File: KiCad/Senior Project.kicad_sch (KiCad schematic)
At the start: 16 parts, among them J1 USB_C_Receptacle_USB2.0_16P, J2 Screw_Terminal_01x02, J3 Screw_Terminal_01x06, J4 Conn_ARM_JTAG_SWD_10, SW1 SW_Push, U1 ESP32-S3-WROOM-1

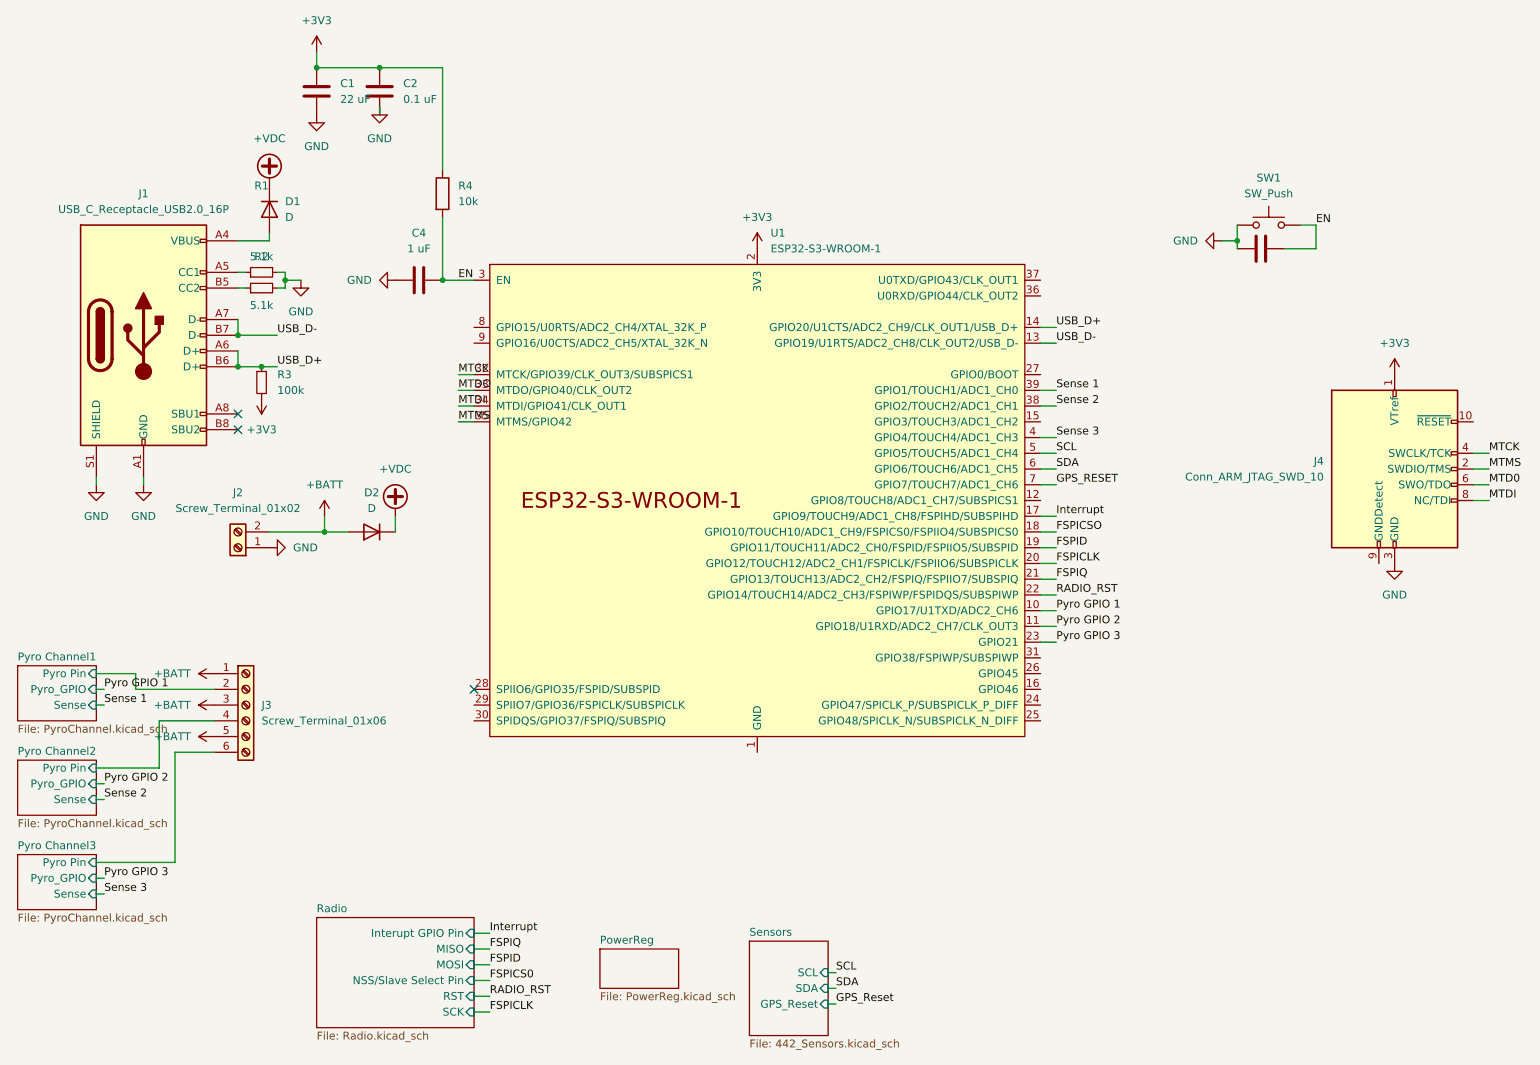
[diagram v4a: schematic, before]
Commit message: Finished base schematic and pin connections, need to add test pins
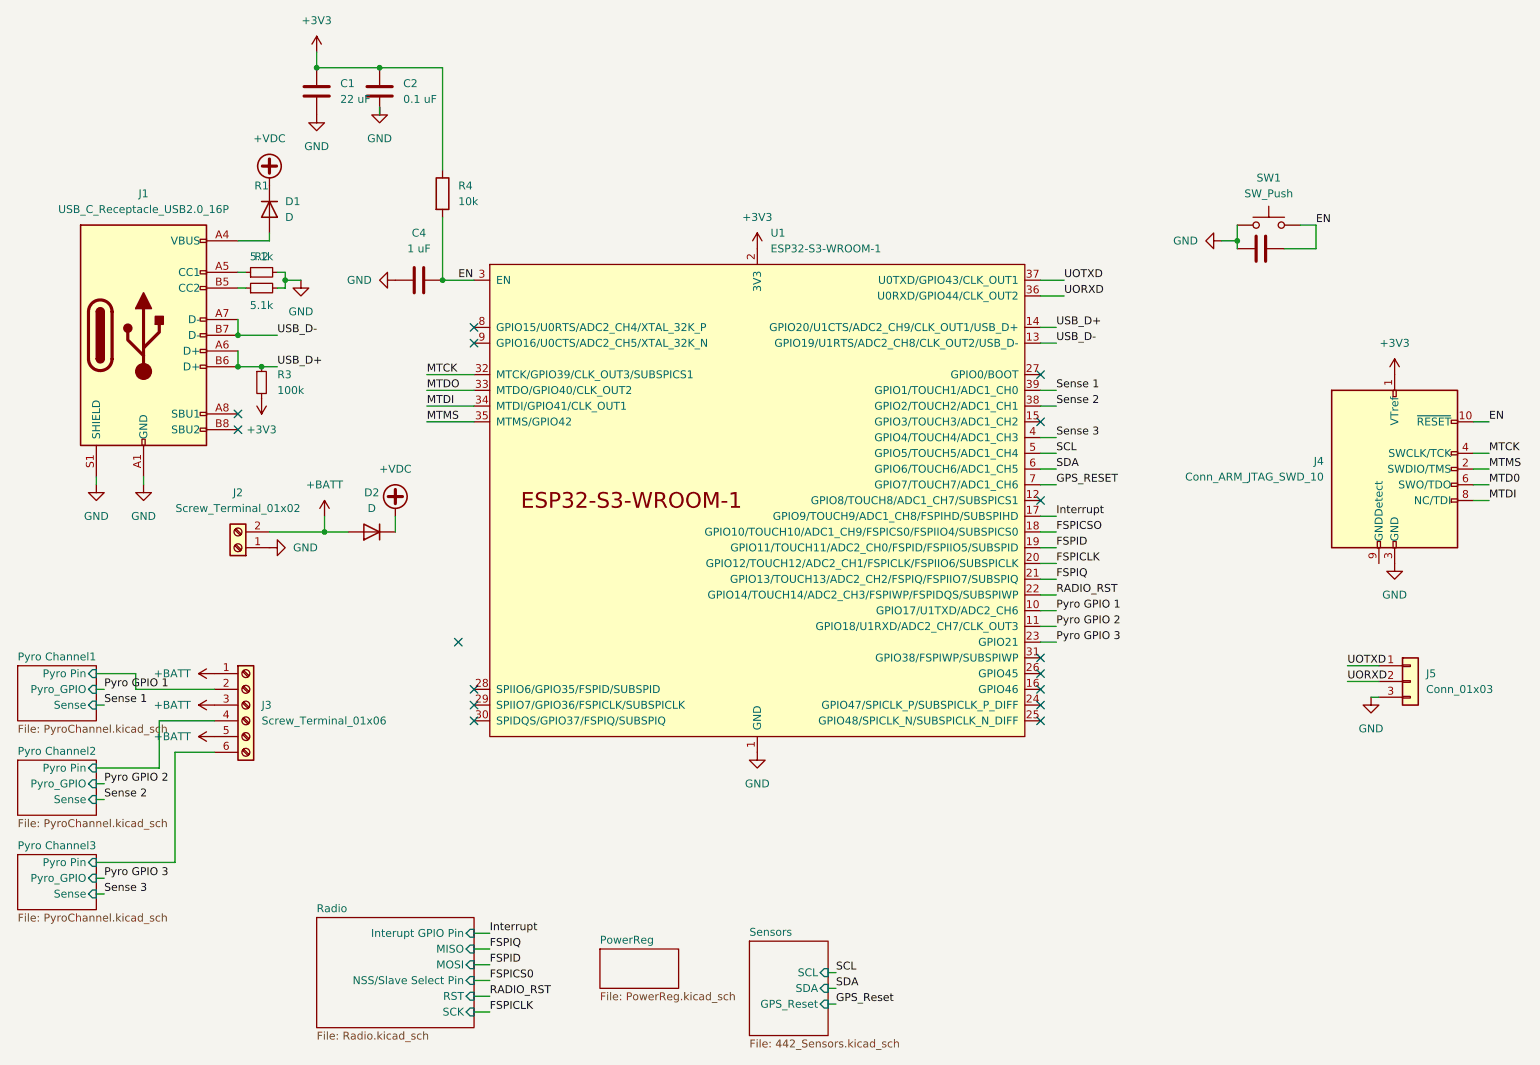
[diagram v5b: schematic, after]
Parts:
- added J5: Conn_01x03, symbol Connector_Generic:Conn_01x03
- J1: footprint Connector_USB:USB_C_Receptacle_JAE_DX07S016JA1R1500 -> USB4105_GF_A (1):GCT_USB4105-GF-A
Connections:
- net EN: now also J4.10 (~{RESET})
- net GND: now also U1.1 (GND), U1.40 (GND), U1.41 (GND), J5.3 (Pin_3)
- net UORXD: now reaches U1.36 (U0RXD/GPIO44/CLK_OUT2)
- net UORXD: now also J5.2 (Pin_2)
- net UOTXD: now reaches U1.37 (U0TXD/GPIO43/CLK_OUT1)
- net UOTXD: now also J5.1 (Pin_1)
- no-connect marks 3 -> 16

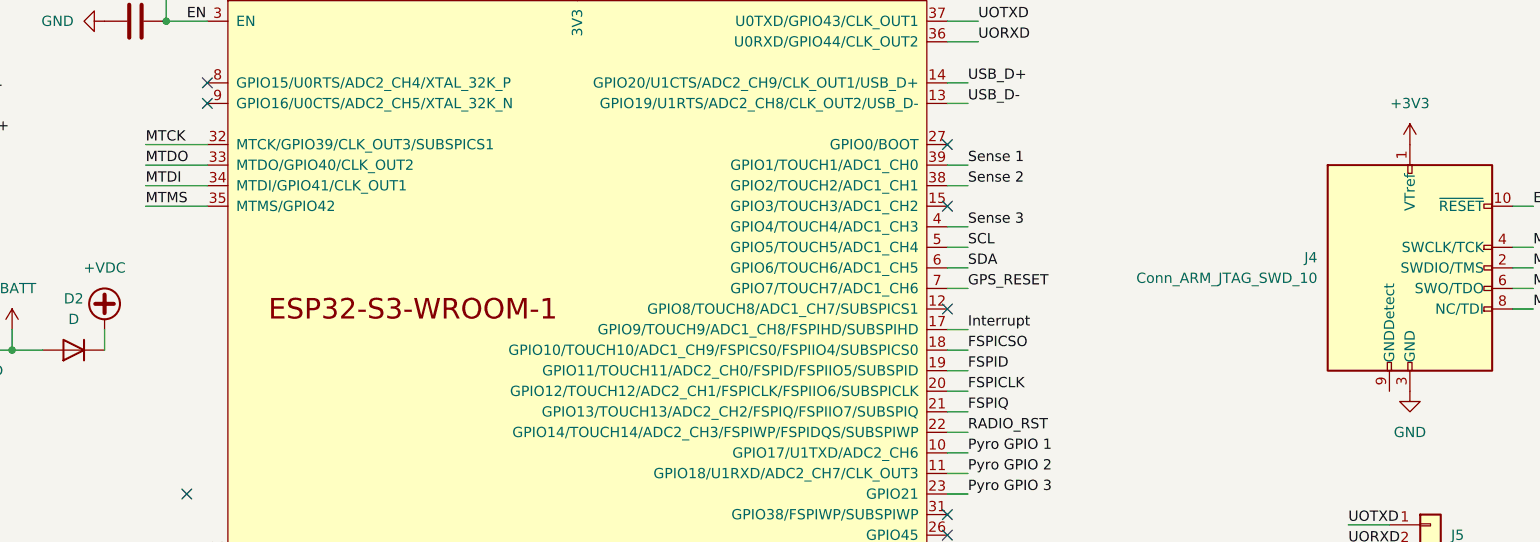
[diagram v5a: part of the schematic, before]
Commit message: ERC fixes and assigned footprints
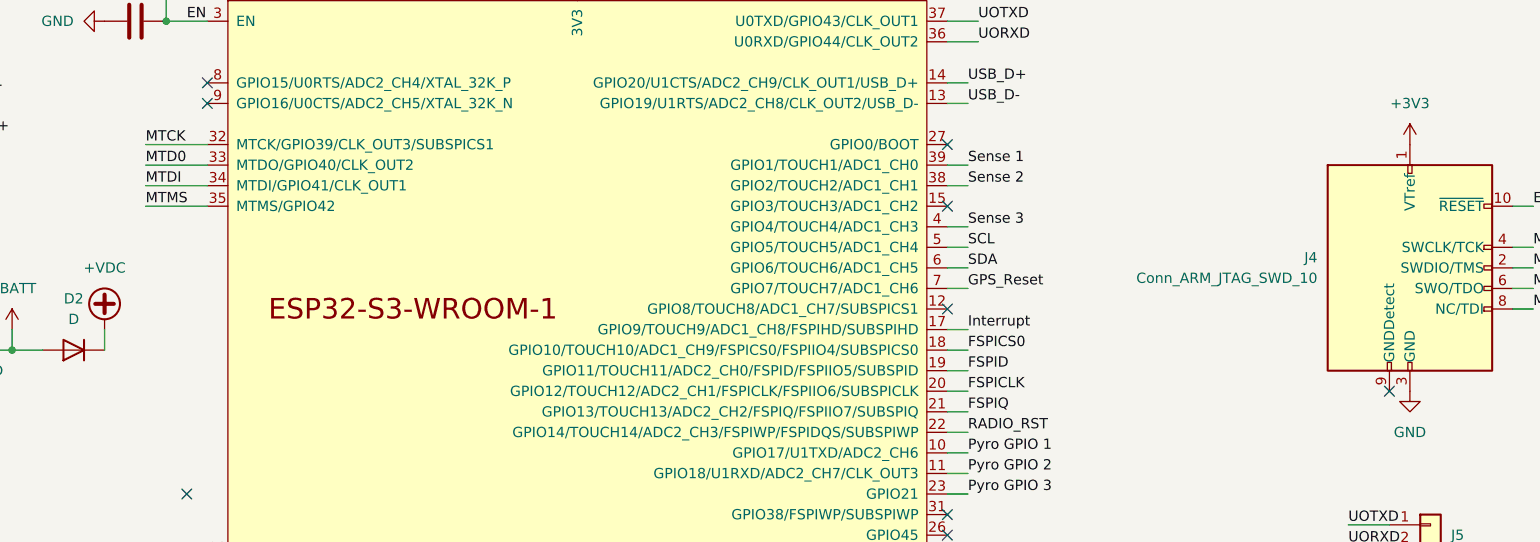
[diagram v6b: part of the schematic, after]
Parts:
- R4: footprint (none) -> Resistor_SMD:R_0402_1005Metric
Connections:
- net FSPICSO is gone; now on net FSPICS0: U1.18 (GPIO10/TOUCH10/ADC1_CH9/FSPICS0/FSPIIO4/SUBSPICS0)
- net GPS_RESET is gone; now on net GPS_Reset: U1.7 (GPIO7/TOUCH7/ADC1_CH6)
- net MTDO is gone; now on net MTD0: U1.33 (MTDO/GPIO40/CLK_OUT2)
- no-connect marks 16 -> 17
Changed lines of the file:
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@@
 	)
 	(no_connect
+		(at 248.92 101.6)
+	)
+	(no_connect
 		(at 102.87 127)
 	)
@@
 	(wire
 		(pts
-			(xy 95.25 73.66) (xy 102.87 73.66)
-		)
-		(stroke
-			(width 0)
-			(type default)
-		)
-	)
-	(wire
-		(pts
 			(xy 41.91 87.63) (xy 41.91 88.9)
 		)
@@
 	(wire
 		(pts
+			(xy 95.25 73.66) (xy 102.87 73.66)
+		)
+		(stroke
+			(width 0)
+			(type default)
+		)
+	)
+	(wire
+		(pts
 			(xy 69.85 48.26) (xy 69.85 49.53)
 		)
@@
 		)
 	)
+	(label "MTD0"
+		(at 95.25 73.66 0)
+		(effects
+			(font
+				(size 1.27 1.27)
+			)
+			(justify left bottom)
+		)
+	)
 	(label "MTCK"
 		(at 95.25 71.12 0)
@@
 		)
 	)
-	(label "GPS_RESET"
+	(label "GPS_Reset"
 		(at 196.85 88.9 0)
 		(effects
@@
 		)
 	)
-	(label "MTDO"
-		(at 95.25 73.66 0)
-		(effects
-			(font
-				(size 1.27 1.27)
-			)
-			(justify left bottom)
-		)
-	)
 	(label "MTMS"
 		(at 95.25 78.74 0)
@@
 		)
 	)
-	(label "FSPICSO"
+	(label "FSPICS0"
 		(at 196.85 96.52 0)
 		(effects
@@
 			)
 		)
-		(property "Footprint" ""
+		(property "Footprint" "Resistor_SMD:R_0402_1005Metric"
 			(at 96.012 41.91 90)
 			(effects

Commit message: More footprints assigned
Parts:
- C1, C2, C3, C4: footprint (none) -> Capacitor_SMD:C_0402_1005Metric
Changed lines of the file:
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@@
 			)
 		)
-		(property "Footprint" ""
+		(property "Footprint" "Capacitor_SMD:C_0402_1005Metric"
 			(at 78.4352 29.21 0)
 			(effects
@@
 			)
 		)
-		(property "Footprint" ""
+		(property "Footprint" "Capacitor_SMD:C_0402_1005Metric"
 			(at 233.68 49.8348 0)
 			(effects
@@
 			)
 		)
-		(property "Footprint" ""
+		(property "Footprint" "Capacitor_SMD:C_0402_1005Metric"
 			(at 97.79 54.9148 0)
 			(effects
@@
 			)
 		)
-		(property "Footprint" ""
+		(property "Footprint" "Capacitor_SMD:C_0402_1005Metric"
 			(at 88.5952 29.21 0)
 			(effects

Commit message: More footprints
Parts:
- SW1: footprint (none) -> Button_Switch_SMD:SW_SPST_PTS810
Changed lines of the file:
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@@
 			)
 		)
-		(property "Footprint" ""
+		(property "Footprint" "Button_Switch_SMD:SW_SPST_PTS810"
 			(at 231.14 41.91 0)
 			(effects
